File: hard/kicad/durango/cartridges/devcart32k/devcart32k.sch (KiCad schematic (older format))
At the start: 9 parts, among them J1 Edge Connector, J2 SD Interface, U1 27/28C256, U2 62256, U4 74HC174, U5 74HC139, U6 74HC245, U7 74HC139

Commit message: finish development cartridge PCB
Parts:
- removed J2: SD Interface, Connector_PinSocket_2.54mm:PinSocket_1x08_P2.54mm_Vertical, symbol Connector_Generic:Conn_01x08
- added J2: SD Interface, Connector_PinHeader_2.54mm:PinHeader_2x08_P2.54mm_Vertical, symbol Connector_Generic:Conn_02x08_Odd_Even
- added LOGO1: Logo_Open_Hardware_Large, Symbol:OSHW-Logo2_24.3x20mm_SilkScreen, symbol Graphic:Logo_Open_Hardware_Large
- added LOGO2: Logo_Open_Hardware_Small, durango:jaqueria, symbol Graphic:Logo_Open_Hardware_Small
- added LOGO3: Logo_Open_Hardware_Small, durango:durango-x90, symbol Graphic:Logo_Open_Hardware_Small
- J1: value Edge Connector -> to Computer
- U1: footprint Package_DIP:DIP-28_W15.24mm_Socket -> Socket:DIP_Socket-28_W11.9_W12.7_W15.24_W17.78_W18.5_3M_228-1277-00-0602J
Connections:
- net +5V: now also J2.5 (Pin_5), J2.6 (Pin_6)
- net GND: now also J2.1 (Pin_1), J2.15 (Pin_15), J2.16 (Pin_16), J2.2 (Pin_2)
- net MCLK: now also J2.11 (Pin_11), J2.12 (Pin_12)
- net MISO: now also J2.13 (Pin_13), J2.14 (Pin_14)
- net MOSI: now also J2.10 (Pin_10), J2.9 (Pin_9)
- net ~SSEL: now also J2.7 (Pin_7), J2.8 (Pin_8)
- net ~WE: now also U2.27 (~WE~), U7.4 (O0)
- no-connect marks 17 -> 18
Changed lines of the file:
@@
 F 0 "U1" H 2725 1325 50  0000 C CNN
 F 1 "27/28C256" H 3150 1325 50  0000 C CNN
-F 2 "Package_DIP:DIP-28_W15.24mm_Socket" H 2900 2375 50  0001 C CNN
+F 2 "Socket:DIP_Socket-28_W11.9_W12.7_W15.24_W17.78_W18.5_3M_228-1277-00-0602J" H 2900 2375 50  0001 C CNN
 F 3 "http://ww1.microchip.com/downloads/en/DeviceDoc/doc0015.pdf" H 2900 2375 50  0001 C CNN
 	1    2900 2375
@@
 P 1550 2225
 F 0 "J1" H 1725 3300 50  0000 C CNN
-F 1 "Edge Connector" H 1225 3300 50  0000 C CNN
+F 1 "to Computer" H 1225 3300 50  0000 C CNN
 F 2 "edge_conn:Durango_ROM" H 1250 1225 50  0001 C CNN
 F 3 "" H 1250 1225 50  0001 C CNN
@@
 	2575 7250 3050 7250
 Connection ~ 2575 5375
-$Comp
-L Connector_Generic:Conn_01x08 J2
-U 1 1 63F6CEF4
+Wire Wire Line
+	5950 5750 6700 5750
+Wire Wire Line
+	5950 5050 6700 5050
+NoConn ~ 6700 5150
+Wire Wire Line
+	4950 3725 6650 3725
+Wire Wire Line
+	6650 3725 6650 5250
+Wire Wire Line
+	6650 5250 6700 5250
+Connection ~ 4950 3725
+Text Label 6700 5350 2    50   ~ 0
+~SSEL
+Text Label 6700 5450 2    50   ~ 0
+MOSI
+Text Label 6700 5550 2    50   ~ 0
+MCLK
+Text Label 6700 5650 2    50   ~ 0
+MISO
+$Comp
+L Connector_Generic:Conn_02x08_Odd_Even J2
+U 1 1 63B847A5
 P 6900 5350
-F 0 "J2" H 6980 5342 50  0000 L CNN
-F 1 "SD Interface" H 6980 5251 50  0000 L CNN
-F 2 "Connector_PinSocket_2.54mm:PinSocket_1x08_P2.54mm_Vertical" H 6900 5350 50  0001 C CNN
+F 0 "J2" H 6950 5867 50  0000 C CNN
+F 1 "SD Interface" H 6950 5776 50  0000 C CNN
+F 2 "Connector_PinHeader_2.54mm:PinHeader_2x08_P2.54mm_Vertical" H 6900 5350 50  0001 C CNN
 F 3 "~" H 6900 5350 50  0001 C CNN
 	1    6900 5350
@@
 $EndComp
 Wire Wire Line
-	5950 5750 6700 5750
-Wire Wire Line
-	5950 5050 6700 5050
-NoConn ~ 6700 5150
-Wire Wire Line
-	4950 3725 6650 3725
-Wire Wire Line
-	6650 3725 6650 5250
-Wire Wire Line
-	6650 5250 6700 5250
+	6700 5050 7200 5050
+Connection ~ 6700 5050
+NoConn ~ 7200 5150
+Wire Wire Line
+	6700 5250 7200 5250
+Connection ~ 6700 5250
+Wire Wire Line
+	6700 5350 7200 5350
+Wire Wire Line
+	6700 5450 7200 5450
+Wire Wire Line
+	6700 5550 7200 5550
+Wire Wire Line
+	6700 5650 7200 5650
+Wire Wire Line
+	6700 5750 7200 5750
 Wire Bus Line
 	3550 875  3550 2075
@@
 Wire Bus Line
 	5700 875  5700 4750
-Connection ~ 4950 3725
-Text Label 6700 5350 2    50   ~ 0
-~SSEL
-Text Label 6700 5450 2    50   ~ 0
-MOSI
-Text Label 6700 5550 2    50   ~ 0
-MCLK
-Text Label 6700 5650 2    50   ~ 0
-MISO
+Connection ~ 6700 5750
+$Comp
+L Graphic:Logo_Open_Hardware_Large LOGO1
+U 1 1 63BF327C
+P 10600 1100
+F 0 "LOGO1" H 10600 1600 50  0001 C CNN
+F 1 "Logo_Open_Hardware_Large" H 10600 700 50  0001 C CNN
+F 2 "Symbol:OSHW-Logo2_24.3x20mm_SilkScreen" H 10600 1100 50  0001 C CNN
+F 3 "~" H 10600 1100 50  0001 C CNN
+	1    10600 1100
+	1    0    0    -1
+$EndComp
+$Comp
+L Graphic:Logo_Open_Hardware_Small LOGO2
+U 1 1 63BF61E9
+P 10600 1875
+F 0 "LOGO2" H 10600 2150 50  0001 C CNN
+F 1 "Logo_Open_Hardware_Small" H 10600 1650 50  0001 C CNN
+F 2 "durango:jaqueria" H 10600 1875 50  0001 C CNN
+F 3 "~" H 10600 1875 50  0001 C CNN
+	1    10600 1875
+	1    0    0    -1
+$EndComp
+Text Label 4050 4150 1    50   ~ 0
+~WE
+$Comp
+L Graphic:Logo_Open_Hardware_Small LOGO3
+U 1 1 63C2970C
+P 10600 2400
+F 0 "LOGO3" H 10600 2675 50  0001 C CNN
+F 1 "Logo_Open_Hardware_Small" H 10600 2175 50  0001 C CNN
+F 2 "durango:durango-x90" H 10600 2400 50  0001 C CNN
+F 3 "~" H 10600 2400 50  0001 C CNN
+	1    10600 2400
+	1    0    0    -1
+$EndComp
 $EndSCHEMATC

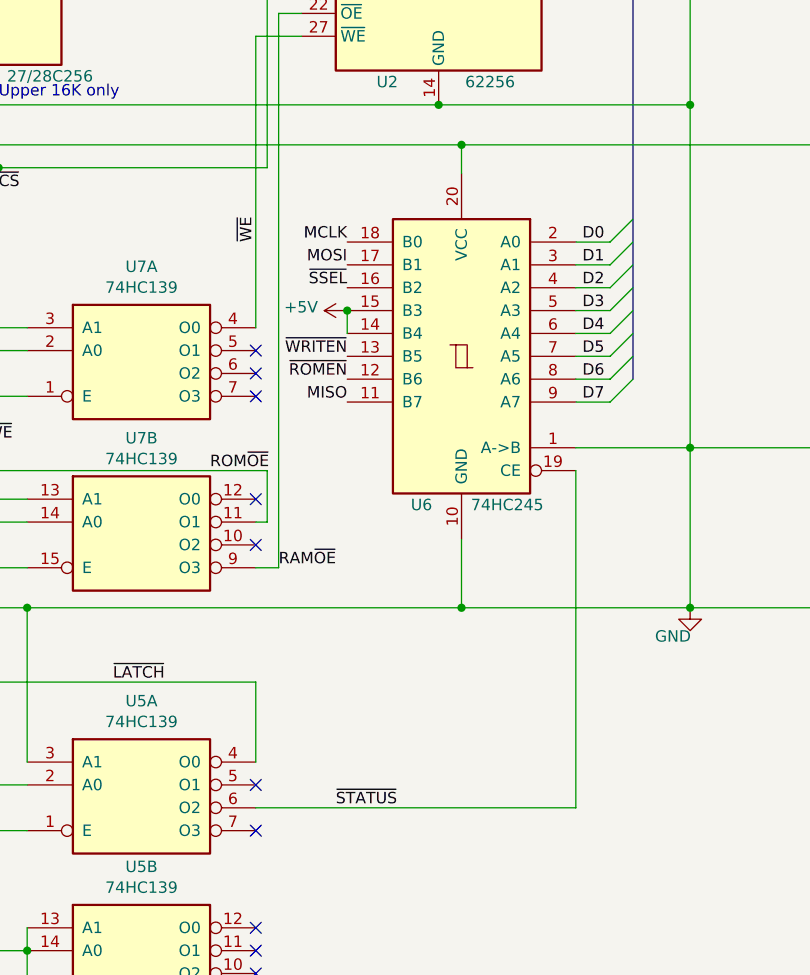
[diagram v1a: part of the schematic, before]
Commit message: fix stupid error in devcart schematic
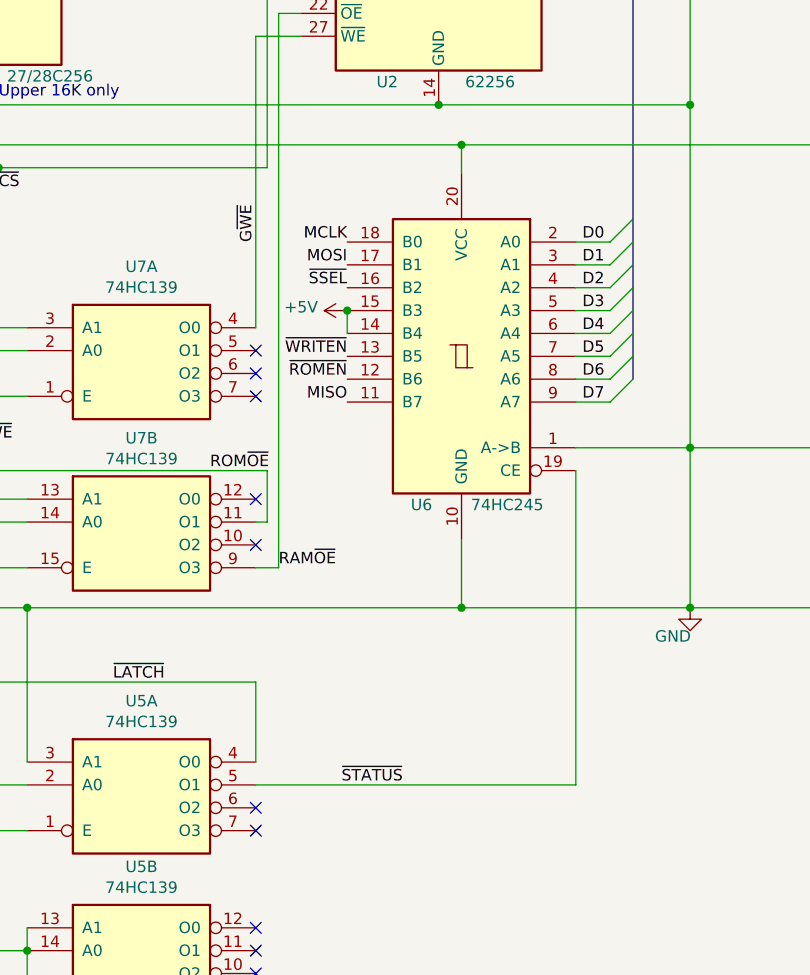
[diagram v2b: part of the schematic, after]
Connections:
- net ~STATUS: now also U5.5 (O1); no longer U5.6 (O2)
- net ~WE: no longer U2.27 (~WE~), U7.4 (O0)
- new net G~WE: U2.27 (~WE~), U7.4 (O0)
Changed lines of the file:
@@
 Wire Wire Line
 	2875 6525 2875 4625
-NoConn ~ 4050 6525
 NoConn ~ 4050 6725
 Wire Wire Line
@@
 MISO
 Wire Wire Line
-	5450 6625 5450 5150
+	5450 6525 5450 5150
 Wire Wire Line
 	5450 5050 5950 5050
@@
 	4050 6425 4050 6075
 Wire Wire Line
-	4050 6625 5450 6625
-Text Label 4400 6625 0    50   ~ 0
+	4050 6525 5450 6525
+Text Label 4425 6525 0    50   ~ 0
 ~STATUS
 Wire Wire Line
@@
 Wire Wire Line
 	6700 5750 7200 5750
-Wire Bus Line
-	3550 875  3550 2075
-Wire Bus Line
-	2225 775  2225 2775
-Wire Bus Line
-	900  875  900  4850
-Wire Bus Line
-	3975 775  3975 2750
-Wire Bus Line
-	5700 875  5700 4750
 Connection ~ 6700 5750
 $Comp
@@
 $EndComp
 Text Label 4050 4150 1    50   ~ 0
-~WE
+G~WE
 $Comp
 L Graphic:Logo_Open_Hardware_Small LOGO3
@@
 	1    0    0    -1
 $EndComp
+NoConn ~ 4050 6625
+Wire Bus Line
+	3550 875  3550 2075
+Wire Bus Line
+	2225 775  2225 2775
+Wire Bus Line
+	900  875  900  4850
+Wire Bus Line
+	3975 775  3975 2750
+Wire Bus Line
+	5700 875  5700 4750
 $EndSCHEMATC

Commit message: fully revised devCart
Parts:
- C1: value 100n -> 22n
- J1: symbol edge_conn:Durango_ROM -> devcart32k-rescue:Durango_ROM-edge_conn
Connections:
- net +5V: no longer U5.13 (A1), U5.14 (A0), U5.15 (E)
- net A3: now also U5.3 (A1)
- net A4: now also U5.14 (A0)
- net A5: now also U5.13 (A1)
- net GND: no longer U5.3 (A1)
- net ~IOC: now also U5.15 (E); no longer U5.1 (E)
- net ~BL0: now reaches U5.12 (O0)
- net ~BL0: now also U5.1 (E)
- no-connect marks 18 -> 17
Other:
- note added: "32 KiB RAM DevCart + SD\n$DFC0-$DFC7"
- note added: "D0 = MCLK\nD1 = MOSI\nD2 = ~SSEL\nD5 = ~WRITEN\nD6 = ~ROMEN\nD7 = MISO"
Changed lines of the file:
@@
 EESchema Schematic File Version 4
-LIBS:devcart32k-cache
-EELAYER 29 0
+EELAYER 30 0
 EELAYER END
 $Descr A4 11693 8268
@@
 P 5000 1150
 F 0 "C1" V 4900 1050 50  0000 C CNN
-F 1 "100n" V 4900 1300 50  0000 C CNN
+F 1 "22n" V 4900 1300 50  0000 C CNN
 F 2 "Capacitor_THT:C_Rect_L7.0mm_W3.5mm_P5.00mm" H 5038 1000 50  0001 C CNN
 F 3 "~" H 5000 1150 50  0001 C CNN
@@
 $EndComp
 $Comp
-L edge_conn:Durango_ROM J1
+L devcart32k-rescue:Durango_ROM-edge_conn J1
 U 1 1 629256A2
 P 1550 2225
@@
 Wire Wire Line
 	2350 3025 2350 3975
-Text Label 2825 6725 2    50   ~ 0
+Text Label 2825 7450 2    50   ~ 0
 ~IOC
 Wire Wire Line
@@
 	2350 3975 2825 3975
 Wire Wire Line
-	2825 3975 2825 6725
-Wire Wire Line
-	2825 6725 3050 6725
+	2825 3975 2825 7450
 $Comp
 L 74xx:74LS139 U5
@@
 $EndComp
 Connection ~ 4450 4450
-Wire Wire Line
-	1650 5750 3050 5750
 $Comp
 L 74xx:74LS139 U7
@@
 Text Label 3850 5150 0    50   ~ 0
 ROM~OE
-Wire Wire Line
-	3050 6425 3050 5750
-Connection ~ 3050 5750
-Wire Wire Line
-	3050 5750 4950 5750
 $Comp
 L 74xx:74LS139 U7
@@
 Wire Wire Line
 	2575 3725 1650 3725
-NoConn ~ 4050 7150
 NoConn ~ 4050 7250
 NoConn ~ 4050 7350
 NoConn ~ 4050 7450
-Wire Wire Line
-	3050 7450 3050 7250
-Connection ~ 3050 7250
-Wire Wire Line
-	3050 7250 3050 7150
-Wire Wire Line
-	2575 5375 2575 7250
-Wire Wire Line
-	2575 7250 3050 7250
-Connection ~ 2575 5375
 Wire Wire Line
 	5950 5750 6700 5750
@@
 $EndComp
 NoConn ~ 4050 6625
+Wire Wire Line
+	2825 7450 3050 7450
+Wire Wire Line
+	1650 5750 4950 5750
+Wire Wire Line
+	3050 6725 3050 6925
+Wire Wire Line
+	3050 6925 4050 6925
+Wire Wire Line
+	4050 6925 4050 7150
 Wire Bus Line
 	3550 875  3550 2075
@@
 Wire Bus Line
 	5700 875  5700 4750
+Text Label 3050 6425 2    50   ~ 0
+A3
+Text Label 3050 7150 2    50   ~ 0
+A5
+Text Label 3050 7250 2    50   ~ 0
+A4
+Text Label 4050 7050 0    50   ~ 0
+~BL0
+Text Notes 5950 2875 0    200  ~ 40
+32 KiB RAM DevCart + SD\n$DFC0-$DFC7
+Text Notes 6700 4725 0    100  ~ 20
+D0 = MCLK\nD1 = MOSI\nD2 = ~SSEL\nD5 = ~WRITEN\nD6 = ~ROMEN\nD7 = MISO
 $EndSCHEMATC

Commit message: faster timing and cleanup for DevCart
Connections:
- net A3: now also U5.15 (E); no longer U5.3 (A1)
- net ~BL0: now also U5.3 (A1); no longer U5.1 (E)
- net ~IOC: now also U5.1 (E); no longer U5.15 (E)
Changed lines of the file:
@@
 Wire Wire Line
 	2350 3025 2350 3975
-Text Label 2825 7450 2    50   ~ 0
+Text Label 2825 6725 2    50   ~ 0
 ~IOC
 Wire Wire Line
@@
 Wire Wire Line
 	2350 3975 2825 3975
-Wire Wire Line
-	2825 3975 2825 7450
 $Comp
 L 74xx:74LS139 U5
@@
 NoConn ~ 4050 6625
 Wire Wire Line
-	2825 7450 3050 7450
-Wire Wire Line
 	1650 5750 4950 5750
 Wire Wire Line
-	3050 6725 3050 6925
-Wire Wire Line
-	3050 6925 4050 6925
+	3000 6925 4050 6925
 Wire Wire Line
 	4050 6925 4050 7150
-Wire Bus Line
-	3550 875  3550 2075
-Wire Bus Line
-	2225 775  2225 2775
-Wire Bus Line
-	900  875  900  4850
-Wire Bus Line
-	3975 775  3975 2750
-Wire Bus Line
-	5700 875  5700 4750
-Text Label 3050 6425 2    50   ~ 0
+Text Label 3050 7450 2    50   ~ 0
 A3
 Text Label 3050 7150 2    50   ~ 0
@@
 Text Notes 6700 4725 0    100  ~ 20
 D0 = MCLK\nD1 = MOSI\nD2 = ~SSEL\nD5 = ~WRITEN\nD6 = ~ROMEN\nD7 = MISO
+Wire Wire Line
+	3000 6925 3000 6425
+Wire Wire Line
+	3000 6425 3050 6425
+Wire Wire Line
+	3050 6725 2825 6725
+Wire Wire Line
+	2825 3975 2825 6725
+Wire Bus Line
+	3550 875  3550 2075
+Wire Bus Line
+	2225 775  2225 2775
+Wire Bus Line
+	900  875  900  4850
+Wire Bus Line
+	3975 775  3975 2750
+Wire Bus Line
+	5700 875  5700 4750
 $EndSCHEMATC

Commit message: updated PCBs
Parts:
- J1: symbol devcart32k-rescue:Durango_ROM-edge_conn -> edge_conn:Durango_ROM
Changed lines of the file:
@@
 EESchema Schematic File Version 4
-EELAYER 30 0
+LIBS:devcart32k-cache
+EELAYER 29 0
 EELAYER END
 $Descr A4 11693 8268
@@
 $EndComp
 $Comp
-L devcart32k-rescue:Durango_ROM-edge_conn J1
+L edge_conn:Durango_ROM J1
 U 1 1 629256A2
 P 1550 2225
